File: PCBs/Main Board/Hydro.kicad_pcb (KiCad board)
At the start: 2 copper layers, 135.4 x 78.7 mm, 46 parts, among them J1 S2P-VHLFSN, J10 43650-0401, J11 436500301, J12 S2P-VHLFSN, J2 S2P-VHLFSN, J3 S2P-VHLFSN, J4 S2P-VHLFSN, J5 S2P-VHLFSN, J6 S2P-VHLFSN, J7 S2P-VHLFSN, J8 436500301, J9 436500301, Q1 FQP30N06L, Q2 FQP30N06L, Q3 FQP30N06L, Q4 FQP30N06L, Q5 FQP30N06L, Q6 FQP30N06L, Q7 FQP30N06L, U1 19p_Header, U2 Tactile_Button, U3 ESP32_WROOM-32U, U4 19p_Header, U5 0.91_OLED, U6 173010378

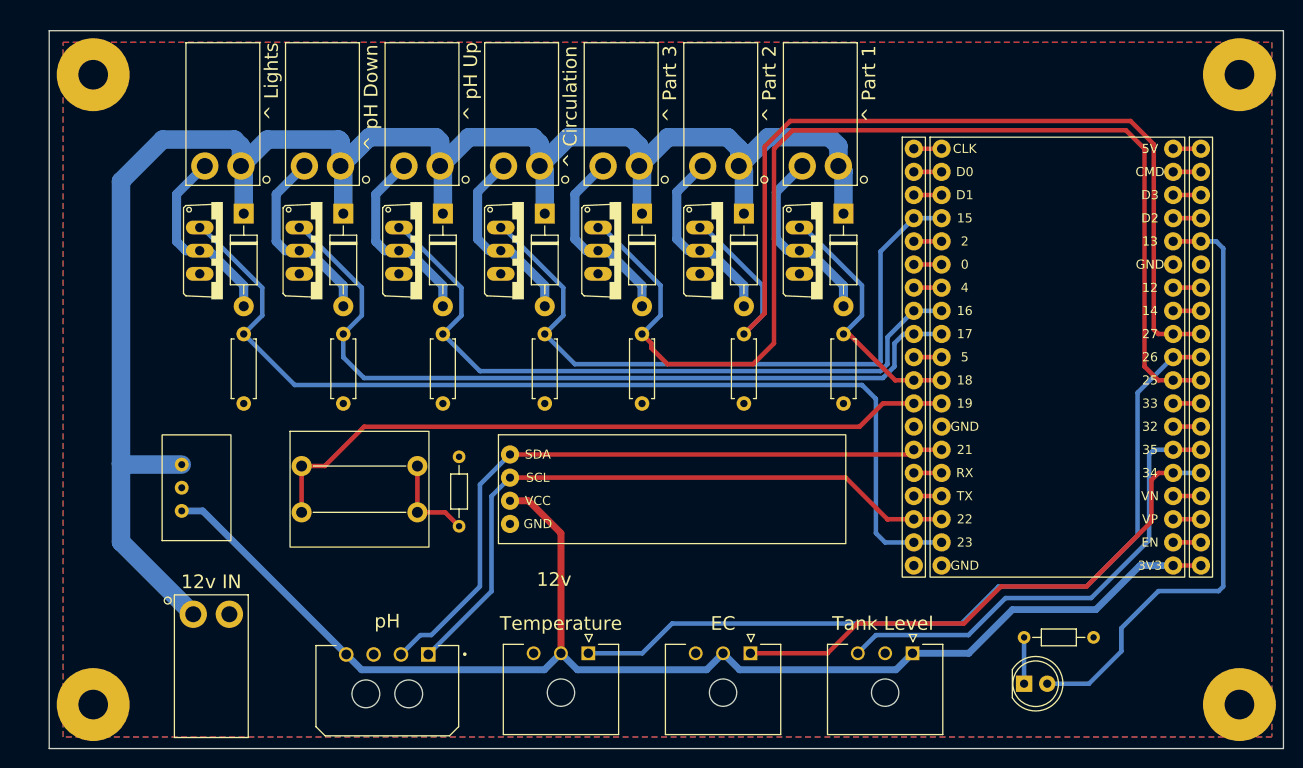
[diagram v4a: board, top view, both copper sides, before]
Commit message: changed semaphore wait to ms
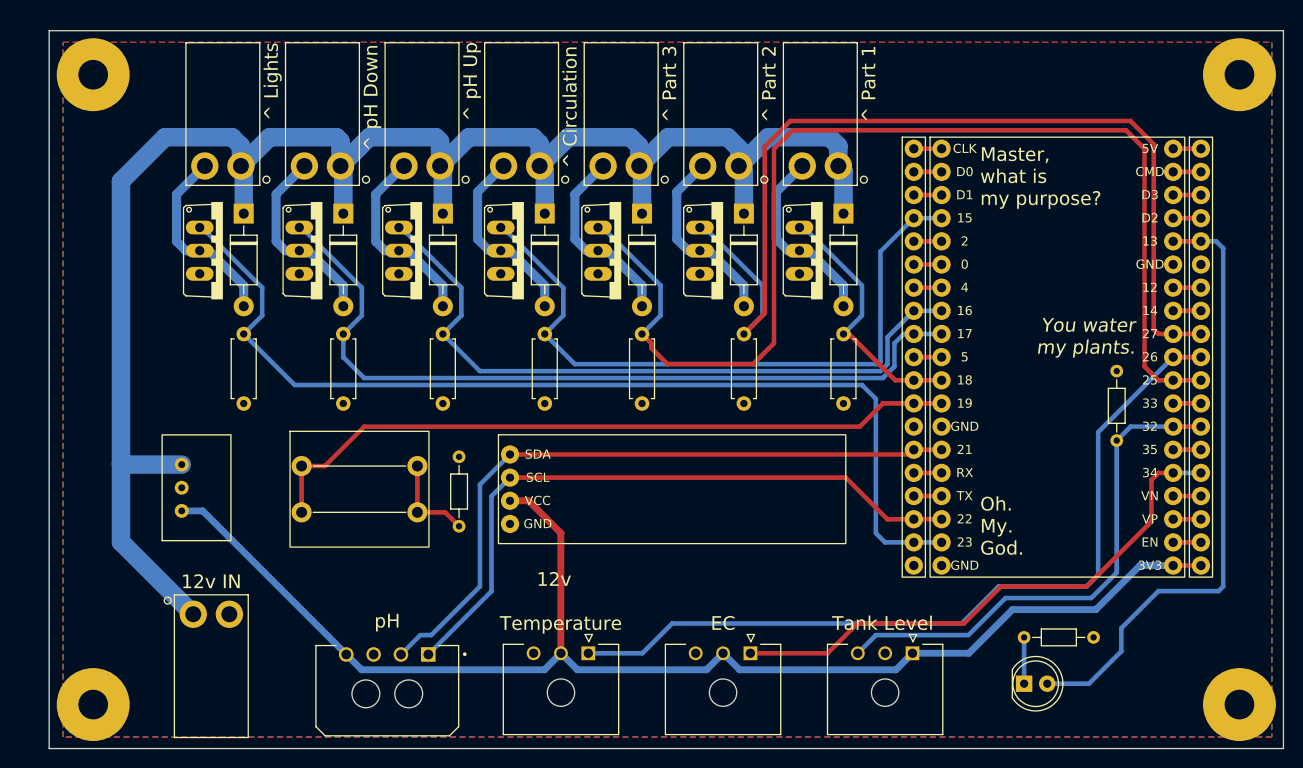
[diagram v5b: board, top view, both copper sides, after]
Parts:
- added R9: R_Small_US, Resistor_THT:R_Axial_DIN0204_L3.6mm_D1.6mm_P7.62mm_Horizontal, F.Cu at (215.4, 79.2)
- renumbered R9 to R10
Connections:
- U3 pad 32: Net-(U3-Pad32) -> waterLevel
- U3 pad 33: waterLevel -> Net-(U3-Pad33)
- U4 pad 13: Net-(U3-Pad32) -> waterLevel
- U4 pad 14: waterLevel -> Net-(U3-Pad33)
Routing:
- net waterLevel: track 52.4 -> 56.4 mm
- net Net-(U3-Pad33): track 0.00 -> 3.05 mm
- net Net-(U3-Pad32): track 3.05 -> 0.00 mm
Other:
- board text added: "Master, what is my purpose?"
- board text added: "Oh. My. God."
- board text added: "You water my plants."

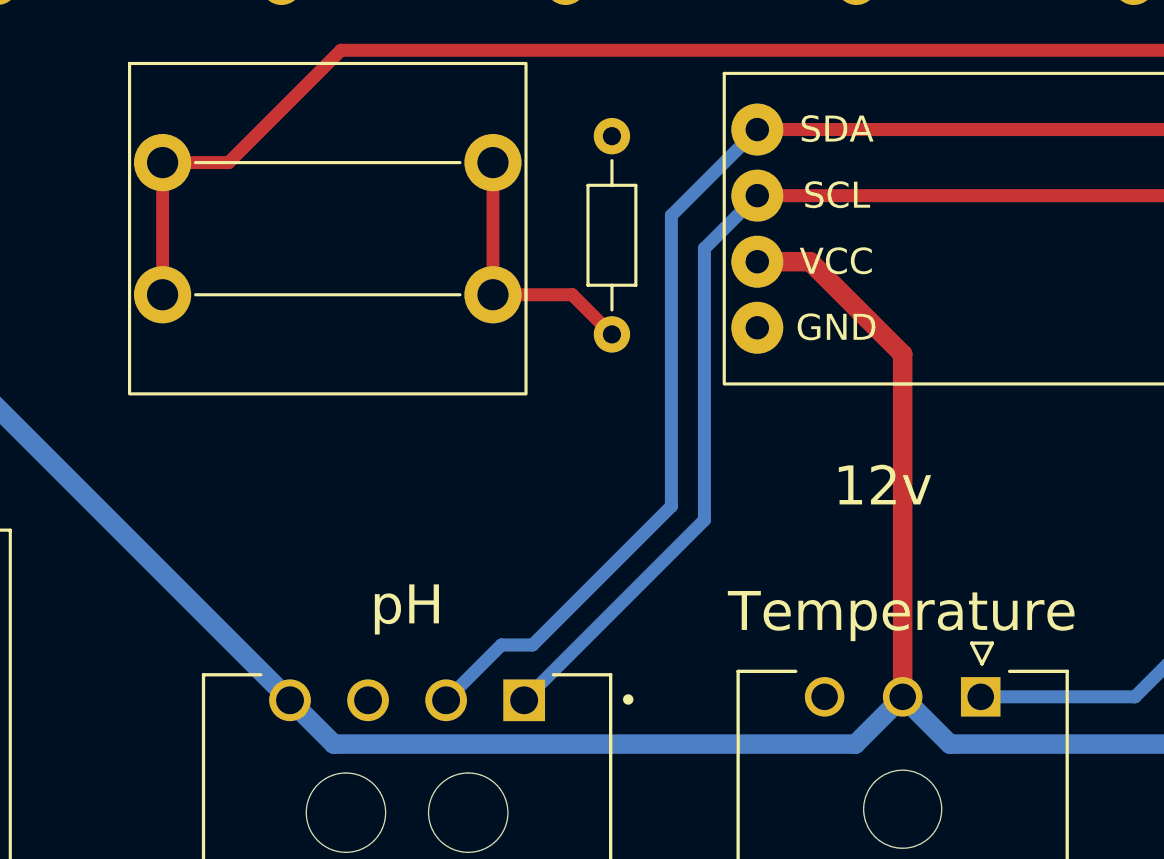
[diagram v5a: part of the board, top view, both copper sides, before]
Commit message: Changes to PCB, wired sensors to board
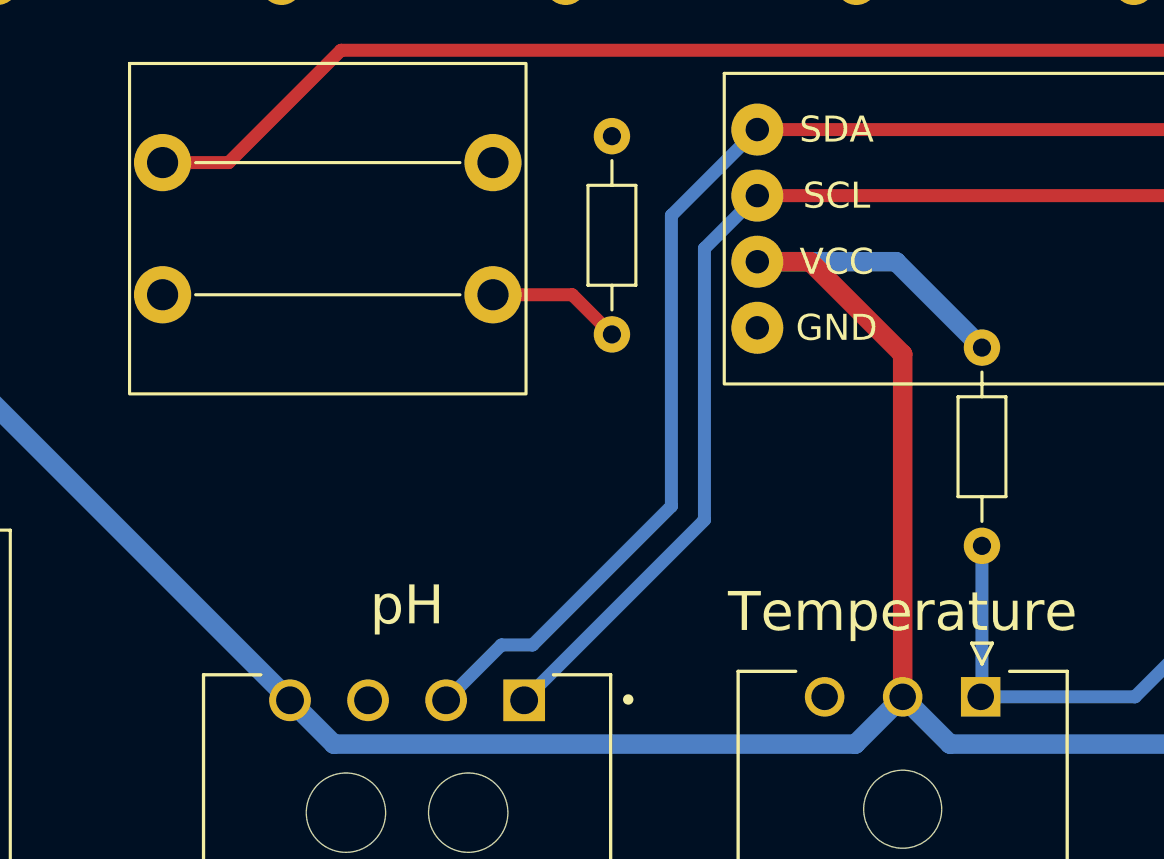
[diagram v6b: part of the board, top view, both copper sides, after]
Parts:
- added R11: 4.7k, Resistor_THT:R_Axial_DIN0204_L3.6mm_D1.6mm_P7.62mm_Horizontal, F.Cu at (157.5, 96.8)
- R9: value R_Small_US -> 10k
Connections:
- U2 pad 2: Net-(U1-Pad12) -> unconnected-(U2-Pad2)
- U2 pad 3: Net-(R8-Pad1) -> unconnected-(U2-Pad3)
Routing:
- net 3V3: track 147.0 -> 157.0 mm
- net tempSignal: track 89.8 -> 95.7 mm
- net Net-(U1-Pad12): track 78.1 -> 73.0 mm
- net Net-(R8-Pad1): track 10.3 -> 5.20 mm
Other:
- board text removed: "12v"
